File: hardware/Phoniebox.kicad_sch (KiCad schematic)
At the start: 8 parts, among them J1 GPIO, J2 Screw_Terminal_01x08, J3 Screw_Terminal_01x08, J4 Screw_Terminal_01x08, J5 Conn_02x02_Odd_Even, J7 USB_B_Micro, J8 Conn_02x04_Odd_Even, U4 CAT24C128

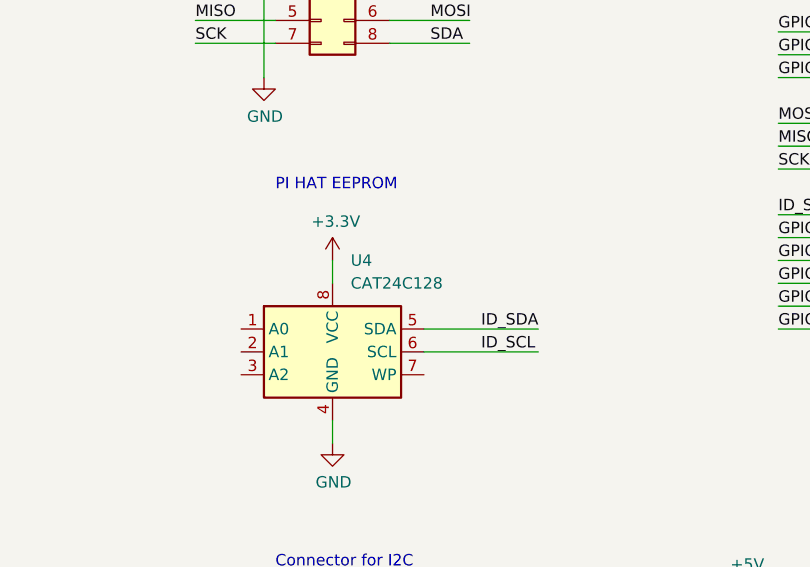
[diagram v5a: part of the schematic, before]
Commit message: Add BOM descriptions and JLC PCB LCSC part numbers. Generate gerber, drill and pick-and-place files.
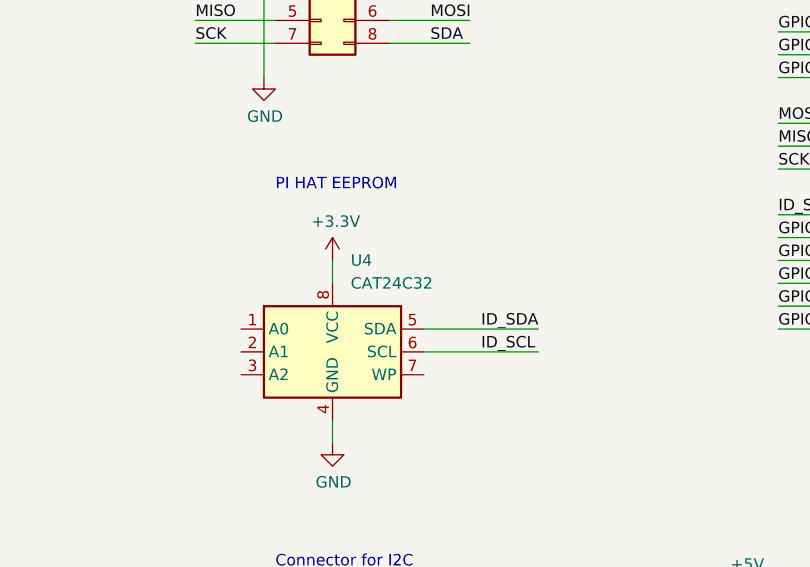
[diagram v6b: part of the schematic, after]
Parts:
- U4: value CAT24C128 -> CAT24C32; Comment (none) -> CAT24C32YI-GT3; LCSC (none) -> C94264
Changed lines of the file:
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@@
       (effects (font (size 1.27 1.27)) (justify left))
     )
-    (property "Value" "CAT24C128" (id 1) (at 153.1494 71.12 0)
+    (property "Value" "CAT24C32" (id 1) (at 153.1494 71.12 0)
       (effects (font (size 1.27 1.27)) (justify left))
     )
@@
     )
     (property "Datasheet" "https://www.onsemi.com/pub/Collateral/CAT24C128-D.PDF" (id 3) (at 151.13 78.74 0)
+      (effects (font (size 1.27 1.27)) hide)
+    )
+    (property "Comment" "CAT24C32YI-GT3" (id 4) (at 151.13 78.74 0)
+      (effects (font (size 1.27 1.27)) hide)
+    )
+    (property "LCSC" "C94264" (id 5) (at 151.13 78.74 0)
       (effects (font (size 1.27 1.27)) hide)
     )
@@
     )
     (path "/9e4892c1-dc01-406a-a6e5-c229f8787227/8d87f6ef-34eb-4ff4-b48c-e0a328c38cfc"
-      (reference "C24") (unit 1) (value "2u2") (footprint "Capacitor_SMD:C_0603_1608Metric_Pad1.08x0.95mm_HandSolder")
+      (reference "C24") (unit 1) (value "4u7") (footprint "Capacitor_SMD:C_0603_1608Metric_Pad1.08x0.95mm_HandSolder")
     )
     (path "/9e4892c1-dc01-406a-a6e5-c229f8787227/24bace7c-8dd5-4c3d-9438-b75e161c55f1"
-      (reference "C25") (unit 1) (value "2u2") (footprint "Capacitor_SMD:C_0603_1608Metric_Pad1.08x0.95mm_HandSolder")
+      (reference "C25") (unit 1) (value "4u7") (footprint "Capacitor_SMD:C_0603_1608Metric_Pad1.08x0.95mm_HandSolder")
     )
     (path "/9e4892c1-dc01-406a-a6e5-c229f8787227/8069f8a0-9a9d-4c5b-b656-c22246293d0c"
@@
     )
     (path "/9169e27c-8c89-42a7-92bd-4526f7962a9a"
-      (reference "U4") (unit 1) (value "CAT24C128") (footprint "Package_SO:TSSOP-8_4.4x3mm_P0.65mm")
-    )
-  )
+      (reference "U4") (unit 1) (value "CAT24C32") (footprint "Package_SO:TSSOP-8_4.4x3mm_P0.65mm")
+    )
+  )

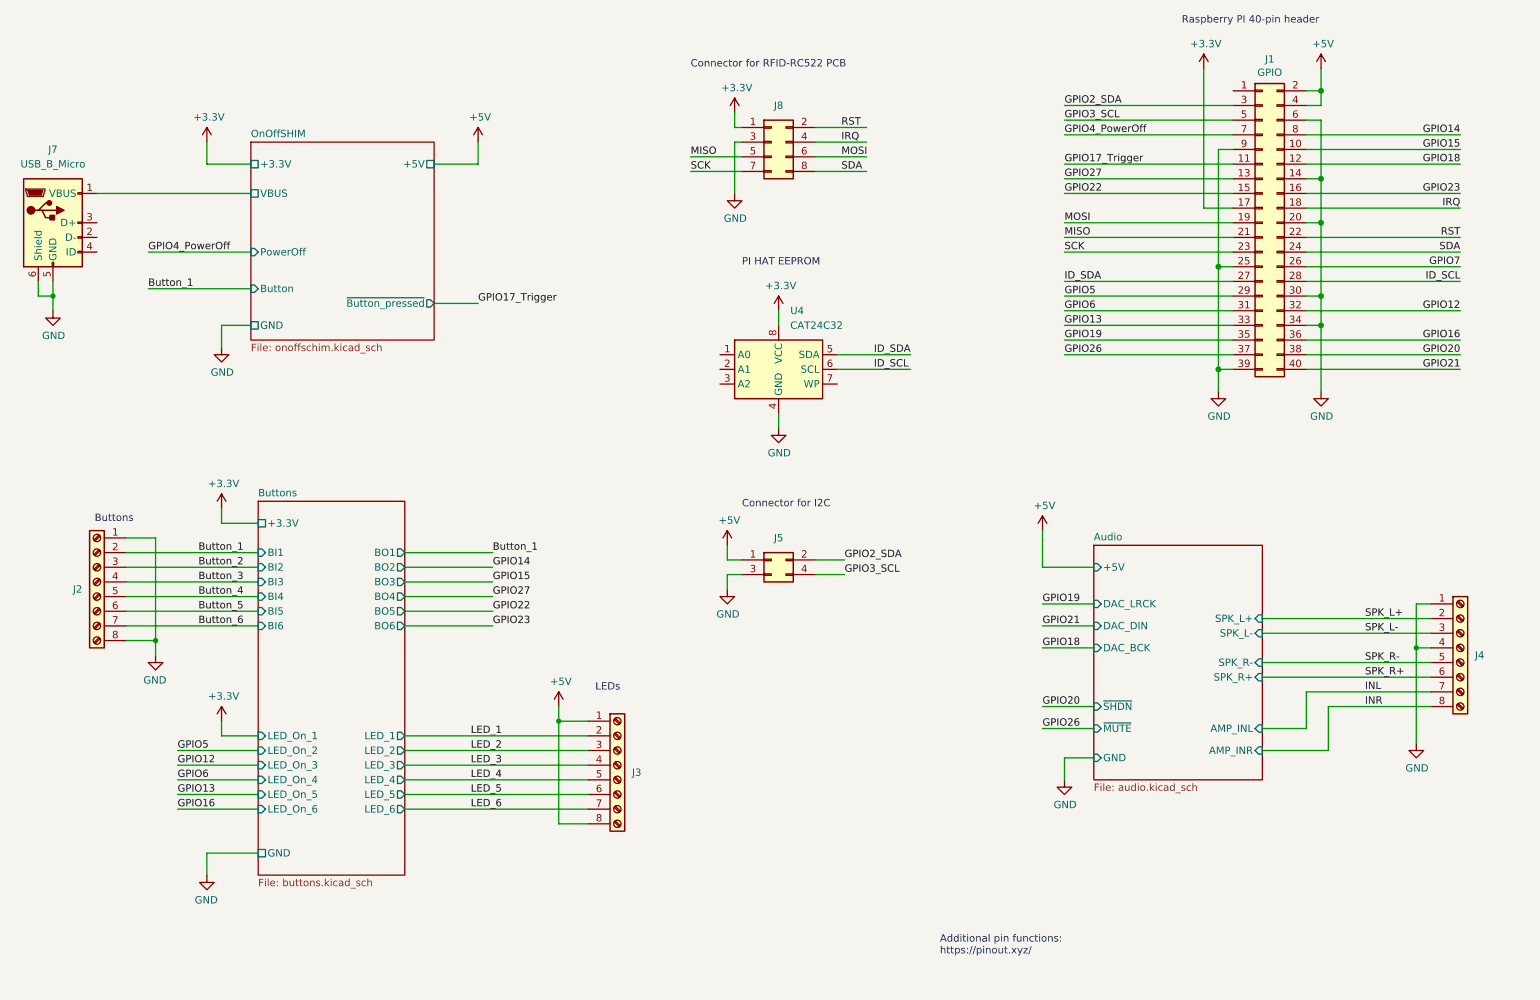
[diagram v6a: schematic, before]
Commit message: Replace micro USB connector with USB-C type connector. DRC errors exist.
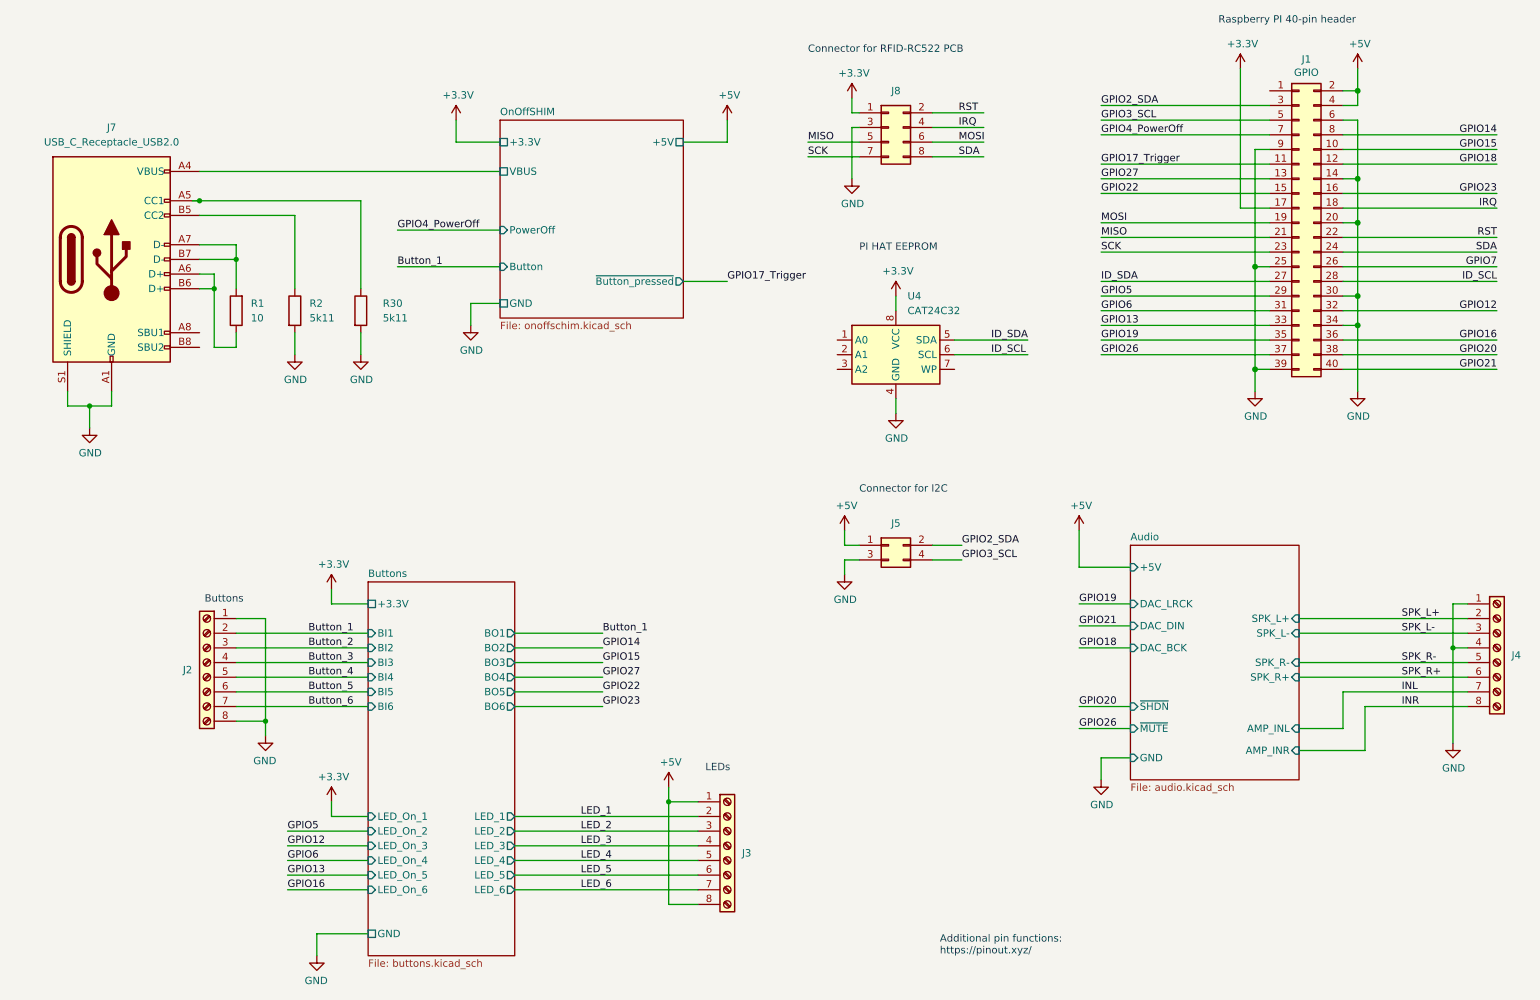
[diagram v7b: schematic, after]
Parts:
- removed J7: USB_B_Micro, Connector_USB:USB_Micro-B_Amphenol_10118194_Horizontal, symbol Connector:USB_B_Micro
- added J7: USB_C_Receptacle_USB2.0, Connector_USB:USB_C_Receptacle_HRO_TYPE-C-31-M-12, symbol Connector:USB_C_Receptacle_USB2.0
- added R1: 10, Resistor_SMD:R_0603_1608Metric_Pad0.98x0.95mm_HandSolder, symbol Device:R
- added R2, R30: 5k11, Resistor_SMD:R_0603_1608Metric_Pad0.98x0.95mm_HandSolder, symbol Device:R
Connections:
- net GND: now also J7.A1 (GND), J7.A12 (GND), J7.B1 (GND), J7.B12 (GND), J7.S1 (SHIELD), R2.2, R30.2
- net OnOffSHIM/VBUS: now also J7.A4 (VBUS), J7.A9 (VBUS), J7.B4 (VBUS), J7.B9 (VBUS)
- new net: J7.A5 (CC1), R30.1
- new net: J7.A6 (D+), J7.B6 (D+), R1.1
- new net: J7.A7 (D-), J7.B7 (D-), R1.2
- new net: J7.B5 (CC2), R2.1
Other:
- moved on the sheet: J1, J2, J3, J4, J5, J8, U4

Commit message: Fixed gridd issues. Properly added USB-C connector. Fixed DRC errors.
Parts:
- J1: Comment (none) -> 2.54-2*20; LCSC (none) -> C2977589
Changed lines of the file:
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@@
+      (effects (font (size 1.27 1.27)) hide)
+    )
+    (property "Comment" "2.54-2*20" (id 4) (at 241.3 53.34 0)
+      (effects (font (size 1.27 1.27)) hide)
+    )
+    (property "LCSC" "C2977589" (id 5) (at 241.3 53.34 0)
       (effects (font (size 1.27 1.27)) hide)
     )
